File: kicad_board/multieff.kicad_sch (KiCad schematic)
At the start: 49 parts, among them J1 Wha1, U1 MCP23017_SO, U2 MCP23017_SO, U3 ADS1115

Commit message: Work in progress
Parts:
- added U4: ADS1115IDGS, Package_SO:TSSOP-10_3x3mm_P0.5mm, symbol Analog_ADC:ADS1115IDGS
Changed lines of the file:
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@@
+	)
+	(symbol
+		(lib_id "Analog_ADC:ADS1115IDGS")
+		(at 240.03 88.9 0)
+		(unit 1)
+		(exclude_from_sim no)
+		(in_bom yes)
+		(on_board yes)
+		(dnp no)
+		(fields_autoplaced yes)
+		(property "Reference" "U4"
+			(at 242.1733 73.66 0)
+			(effects
+				(font
+					(size 1.27 1.27)
+				)
+				(justify left)
+			)
+		)
+		(property "Value" "ADS1115IDGS"
+			(at 242.1733 76.2 0)
+			(effects
+				(font
+					(size 1.27 1.27)
+				)
+				(justify left)
+			)
+		)
+		(property "Footprint" "Package_SO:TSSOP-10_3x3mm_P0.5mm"
+			(at 240.03 101.6 0)
+			(effects
+				(font
+					(size 1.27 1.27)
+				)
+				(hide yes)
+			)
+		)
+		(property "Datasheet" "http://www.ti.com/lit/ds/symlink/ads1113.pdf"
+			(at 238.76 111.76 0)
+			(effects
+				(font
+					(size 1.27 1.27)
+				)
+				(hide yes)
+			)
+		)
+		(property "Description" "Ultra-Small, Low-Power, I2C-Compatible, 860-SPS, 16-Bit ADCs With Internal Reference, Oscillator, and Programmable Comparator, VSSOP-10"
+			(at 240.03 88.9 0)
+			(effects
+				(font
+					(size 1.27 1.27)
+				)
+				(hide yes)
+			)
+		)
+		(pin "1"
+		)
+		(pin "2"
+		)
+		(pin "6"
+		)
+		(pin "3"
+		)
+		(pin "8"
+		)
+		(pin "7"
+		)
+		(pin "5"
+		)
+		(pin "4"
+		)
+		(pin "9"
+		)
+		(pin "10"
+		)
+		(instances
+			(project ""
+				(path "/01a67eee-3893-4e68-bed0-a04a64951ab4"
+					(reference "U4")
+					(unit 1)
+				)
+			)
+		)
 	)
 	(symbol

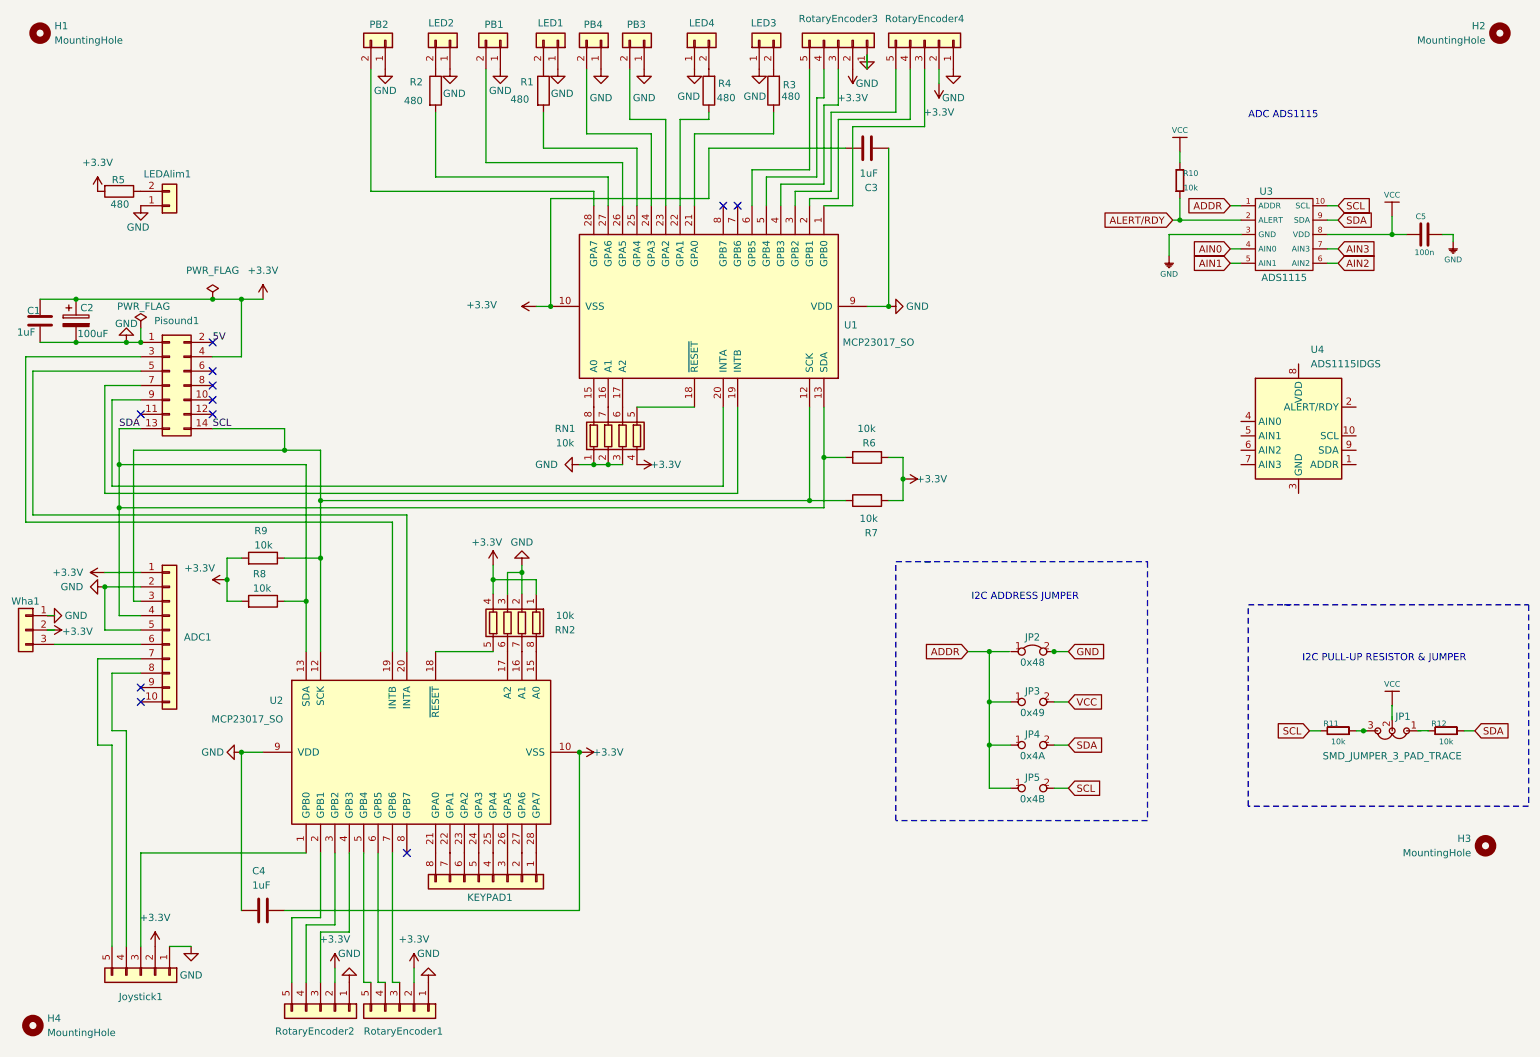
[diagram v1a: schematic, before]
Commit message: First complete IC based version
Still miss some decoupling condensators.
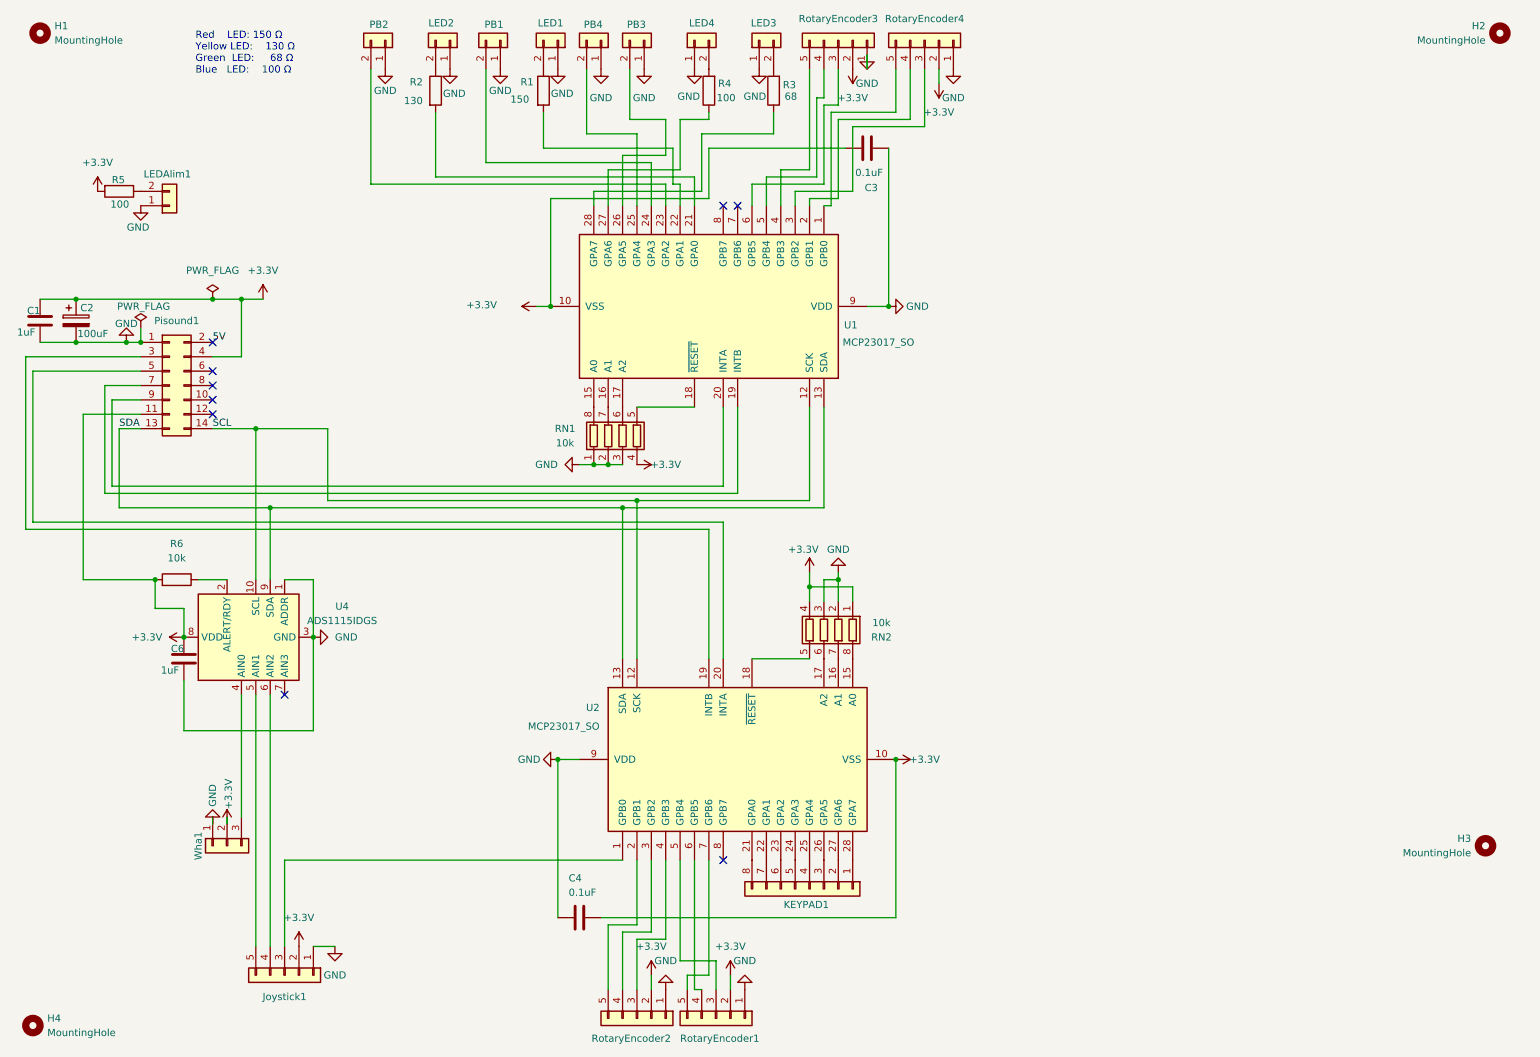
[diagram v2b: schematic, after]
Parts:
- removed ADC1: Conn_01x10, Connector_PinSocket_2.54mm:PinSocket_1x10_P2.54mm_Vertical, symbol Connector_Generic:Conn_01x10
- removed C5: 100n, e-radionica.com footprinti:0603C, symbol e-radionica.com schematics:0603C
- removed JP1: SMD_JUMPER_3_PAD_TRACE, e-radionica.com footprinti:SMD_JUMPER_3_PAD_TRACE, symbol e-radionica.com schematics:SMD_JUMPER_3_PAD_TRACE
- removed JP2: 0x48, e-radionica.com footprinti:SMD_JUMPER_CONNECTED, symbol e-radionica.com schematics:SMD-JUMPER-CONNECTED
- removed JP3: 0x49, e-radionica.com footprinti:SMD_JUMPER, symbol e-radionica.com schematics:SMD_JUMPER
- removed JP4: 0x4A, e-radionica.com footprinti:SMD_JUMPER, symbol e-radionica.com schematics:SMD_JUMPER
- removed JP5: 0x4B, e-radionica.com footprinti:SMD_JUMPER, symbol e-radionica.com schematics:SMD_JUMPER
- removed R10, R11, R12: 10k, e-radionica.com footprinti:0603R, symbol e-radionica.com schematics:0603R
- removed R6, R7, R8, R9: 10k, PCM_Resistor_SMD_AKL:R_1206_3216Metric, symbol PCM_Resistor_AKL:R_1206
- removed U3: ADS1115, e-radionica.com footprinti:VSSOP, symbol e-radionica.com schematics:ADS1115
- added C6: 1uF, Capacitor_THT:C_Disc_D5.0mm_W2.5mm_P2.50mm, symbol Device:C
- added R6: 10k, PCM_Resistor_SMD_AKL:R_0612_1632Metric, symbol PCM_Resistor_AKL:R_0612
- C3, C4: value 1uF -> 0.1uF
- R1: value 480 -> 150
- R2: value 480 -> 130
- R3: value 480 -> 68
- R4, R5: value 480 -> 100
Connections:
- net +3.3V: now also Pisound1.11 (Pin_11), U4.8 (VDD), C6.1, R6.1
- net GND: now also U4.1 (ADDR), U4.3 (GND), C6.2
- net SCL: now also U4.10 (SCL)
- net SDA: now also U4.9 (SDA)
- net at PB3.2 (Pin_2): now also U1.26 (GPA5); no longer U1.23 (GPA2)
- net at U2.5 (GPB4): now also RotaryEncoder1.3 (Pin_3); no longer RotaryEncoder1.5 (Pin_5)
- net at U2.7 (GPB6): now also RotaryEncoder1.5 (Pin_5); no longer RotaryEncoder1.3 (Pin_3)
- net at PB4.2 (Pin_2): now also U1.25 (GPA4); no longer U1.24 (GPA3)
- net at J1.3 (Pin_3): now also U4.4 (AIN0)
- net at Joystick1.5 (Pin_5): now also U4.5 (AIN1)
- net at Joystick1.4 (Pin_4): now also U4.6 (AIN2)
- net at R2.2: now also U1.21 (GPA0); no longer U1.27 (GPA6)
- net at RotaryEncoder4.3 (Pin_3): now also U1.3 (GPB2); no longer U1.1 (GPB0)
- net at RotaryEncoder4.5 (Pin_5): now also U1.1 (GPB0); no longer U1.3 (GPB2)
- net at U4.2 (ALERT/RDY): now also R6.2
- net at R4.1: now also U1.27 (GPA6); no longer U1.22 (GPA1)
- net at PB1.2 (Pin_2): now also U1.24 (GPA3); no longer U1.26 (GPA5)
- net at PB2.2 (Pin_2): now also U1.23 (GPA2); no longer U1.28 (GPA7)
- net at R3.1: now also U1.28 (GPA7); no longer U1.21 (GPA0)
- net at R1.2: now also U1.22 (GPA1); no longer U1.25 (GPA4)
- net at U1.4 (GPB3): now also RotaryEncoder3.5 (Pin_5); no longer RotaryEncoder3.3 (Pin_3)
- net at U1.6 (GPB5): now also RotaryEncoder3.3 (Pin_3); no longer RotaryEncoder3.5 (Pin_5)
- no-connect marks 11 -> 9
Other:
- note added: "Red LED: 150 Ω Yellow LED: 130 Ω Green LED: 68 Ω Blue LED: 100 Ω"
- note removed: "ADC ADS1115"
- note removed: "I2C ADDRESS JUMPER"
- note removed: "I2C PULL-UP RESISTOR & JUMPER"
- moved on the sheet: C4, Joystick1, KEYPAD1, RN2, RotaryEncoder1, RotaryEncoder2, U2, U4

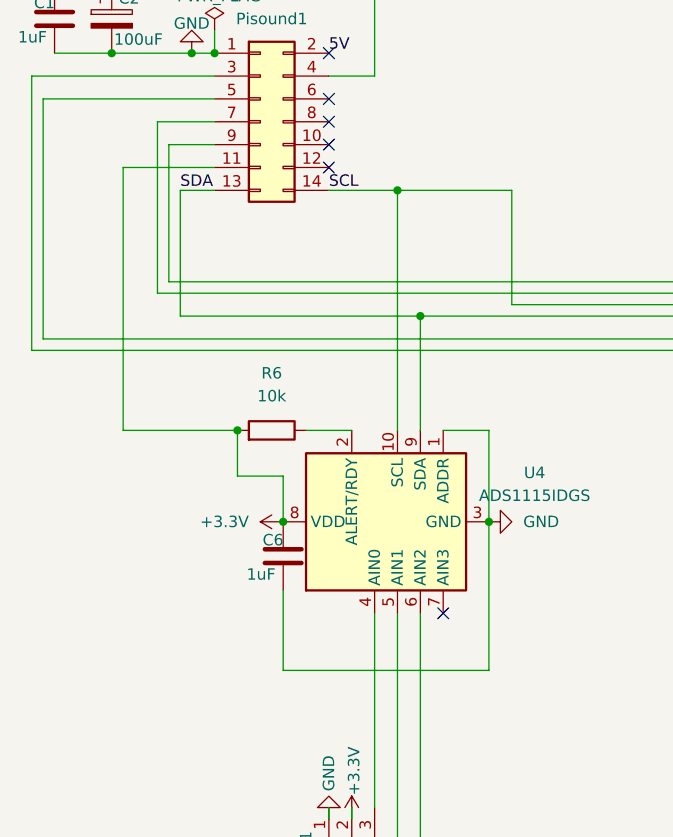
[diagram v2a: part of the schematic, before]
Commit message: Chips decoupling complete
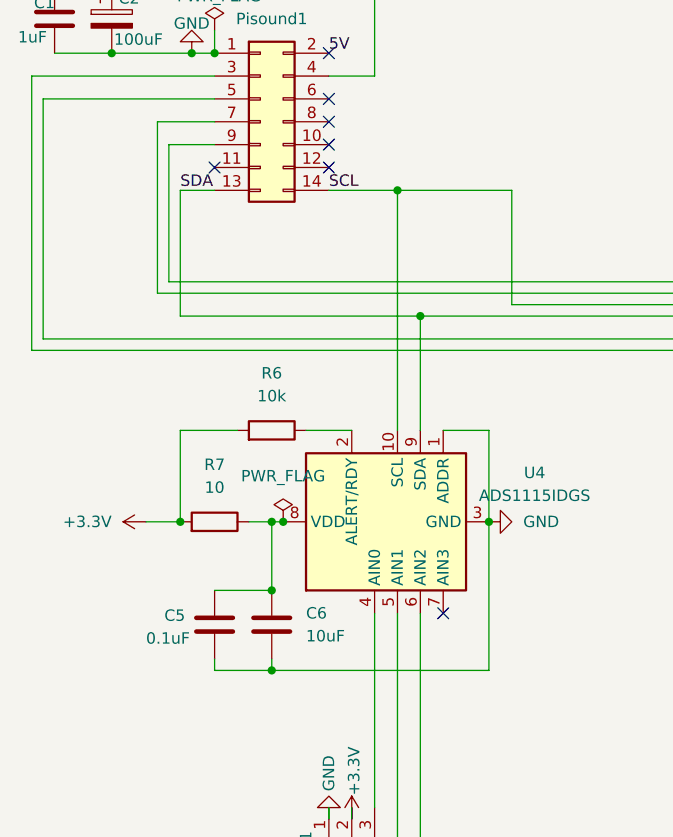
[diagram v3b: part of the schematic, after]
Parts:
- removed C6: 1uF, Capacitor_THT:C_Disc_D5.0mm_W2.5mm_P2.50mm, symbol Device:C
- added C5: 0.1uF, PCM_Capacitor_SMD_AKL:C_0805_2012Metric, symbol PCM_Capacitor_AKL:C_0805
- added C6: 10uF, PCM_Capacitor_SMD_AKL:C_0805_2012Metric, symbol PCM_Capacitor_AKL:C_0805
- added R7: 10, PCM_Resistor_SMD_AKL:R_0612_1632Metric, symbol PCM_Resistor_AKL:R_0612
- C1: footprint Capacitor_THT:C_Disc_D5.0mm_W2.5mm_P2.50mm -> Capacitor_SMD:C_0805_2012Metric
- C2: footprint Capacitor_THT:CP_Radial_D5.0mm_P2.00mm -> Capacitor_SMD:CP_Elec_6.3x5.4
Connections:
- net +3.3V: now also R7.1; no longer Pisound1.11 (Pin_11), U4.8 (VDD)
- net GND: now also C5.2, C6.2
- new net: C5.1, C6.1, R7.2, U4.8 (VDD)
- no-connect marks 9 -> 10
